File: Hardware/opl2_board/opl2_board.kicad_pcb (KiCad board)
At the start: 2 copper layers, 80.8 x 60.1 mm, 21 parts, among them J1 Conn_01x40, J2 AudioJack3, U1 74HC00, U2 YM3812, U3 YM3014B, U4 LM358, X1 CXO_DIP8

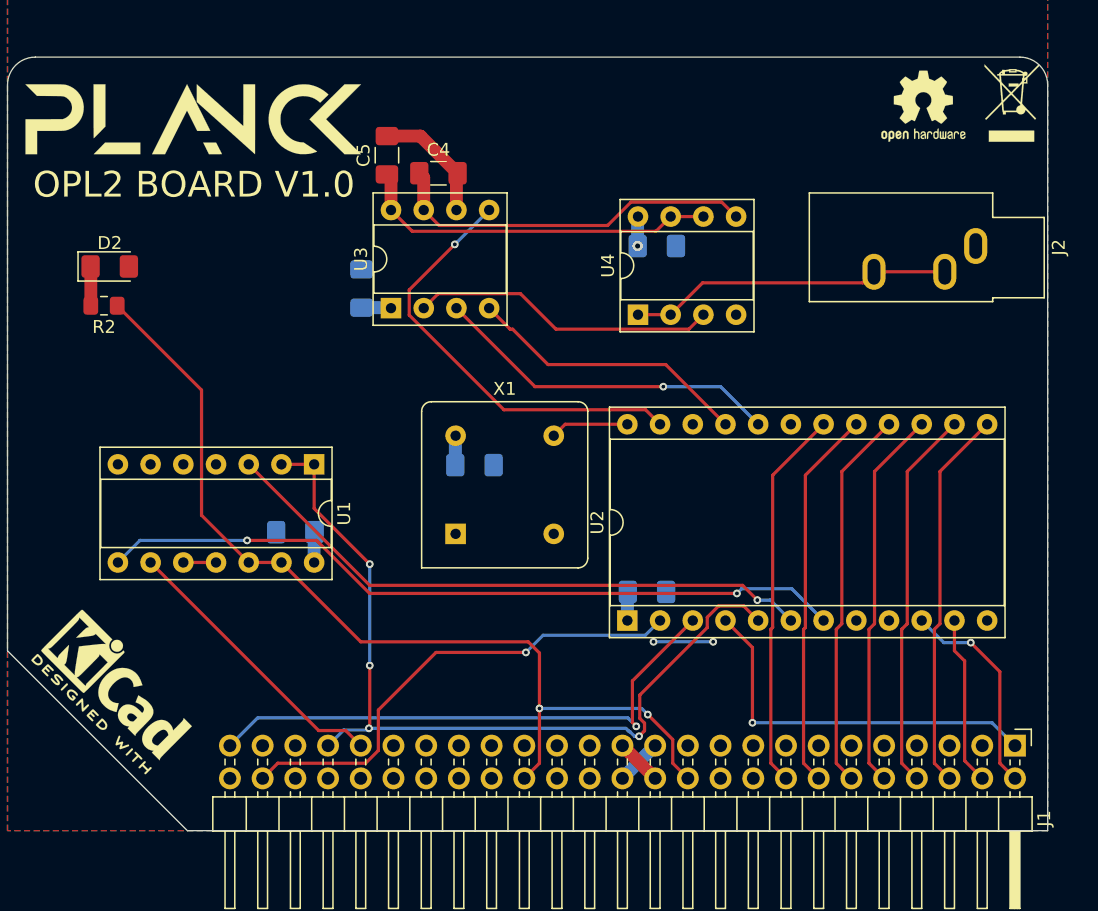
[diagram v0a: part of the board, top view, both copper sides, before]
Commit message: Through hole components for OPL2 board
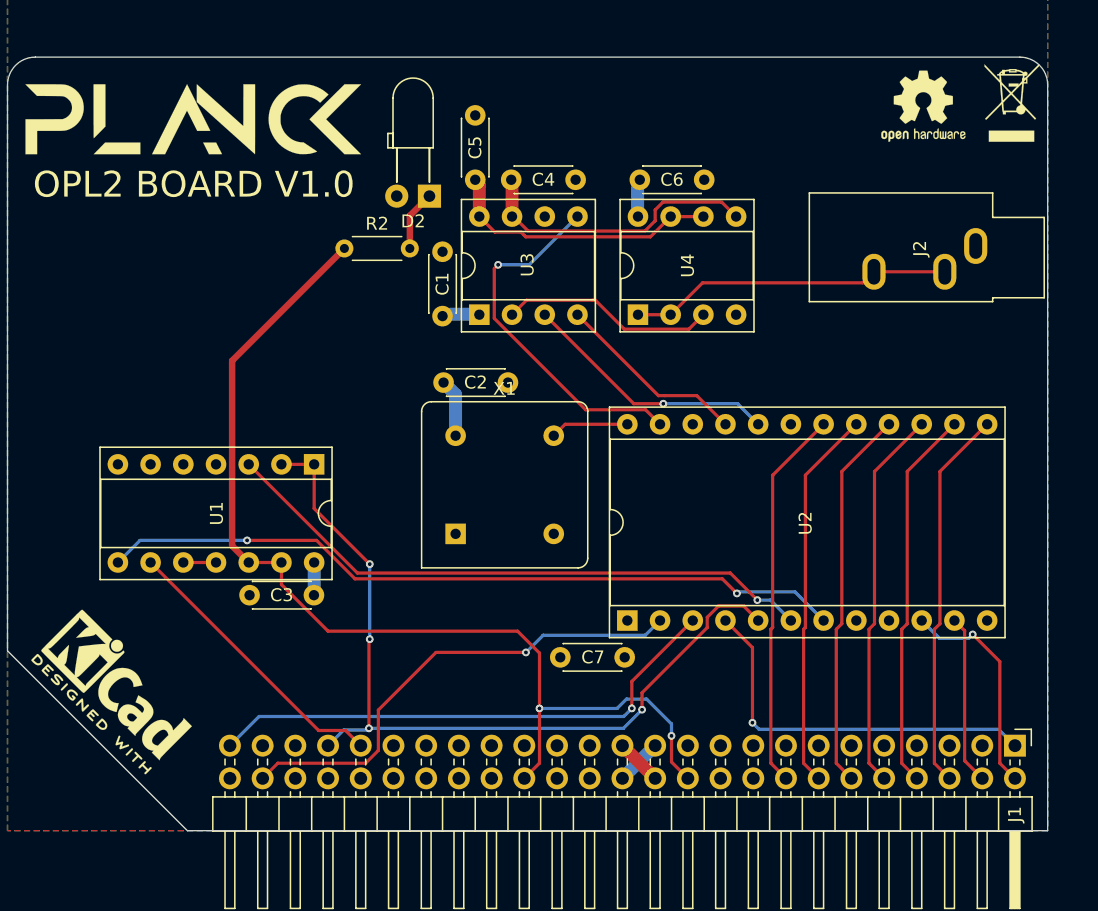
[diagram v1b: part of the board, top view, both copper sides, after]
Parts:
- C1, C2, C3, C6, C7: value C_Small -> 4.7u; footprint Capacitor_SMD:C_1206_3216Metric_Pad1.42x1.75mm_HandSolder -> Capacitor_THT:C_Disc_D4.3mm_W1.9mm_P5.00mm; moved to F.Cu
- C4, C5: footprint Capacitor_SMD:C_1206_3216Metric_Pad1.42x1.75mm_HandSolder -> Capacitor_THT:C_Disc_D4.3mm_W1.9mm_P5.00mm
- D2: footprint LED_SMD:LED_1206_3216Metric_Pad1.42x1.75mm_HandSolder -> LED_THT:LED_D3.0mm_Horizontal_O3.81mm_Z6.0mm
- R2: footprint Resistor_SMD:R_0805_2012Metric_Pad1.15x1.40mm_HandSolder -> Resistor_THT:R_Axial_DIN0204_L3.6mm_D1.6mm_P5.08mm_Horizontal
- X1: value CXO_DIP8 -> 3.579545 MHz
- moved D2 25.4 mm to (32.8, -49.3), turned to 180 degrees
- moved R2 19.2 mm to (26.2, -45.2), turned to 0 degrees
- moved C7 8.43 mm to (42.9, -13.5), turned to 0 degrees
- moved C5 7.12 mm to (36.3, -50.5)
- moved C2 6.92 mm to (38.9, -34.8)
- moved C1 6.91 mm to (33.8, -45.0)
- moved U3 6.88 mm to (36.6, -40.1)
- moved C6 6.33 mm to (54.1, -50.5)
- moved C3 6.05 mm to (18.8, -18.3)
- moved C4 5.67 mm to (39.1, -50.5)
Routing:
- net GND: track 13.2 -> 3.59 mm
- net Net-(U3-Pad2): track 23.8 -> 16.7 mm
- net Net-(U2-Pad21): track 22.1 -> 15.0 mm
- net Net-(U2-Pad20): track 27.2 -> 20.1 mm
- net Net-(C5-Pad1): track 28.3 -> 21.6 mm
- net ~SLOT_SEL~: track 74.7 -> 81.3 mm
- net Net-(C4-Pad1): track 29.0 -> 22.8 mm
- net Net-(U2-Pad23): track 33.7 -> 28.3 mm
- net +5V: track 19.7 -> 15.9 mm, vias 3 -> 0
- net R~W~: track 66.5 -> 64.4 mm
- net ~RESET~: track 43.0 -> 41.2 mm
- net Net-(D2-Pad1): track 3.06 -> 4.70 mm
- net D0: track 16.5 -> 17.2 mm
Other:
- rule pad_to_mask_clearance: 0.05 -> 0

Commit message: bigger resistors on OPL2 board
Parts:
- C1, C2, C3, C6, C7: value 4.7u -> 10n
- R2: footprint Resistor_THT:R_Axial_DIN0204_L3.6mm_D1.6mm_P5.08mm_Horizontal -> Resistor_THT:R_Axial_DIN0207_L6.3mm_D2.5mm_P10.16mm_Horizontal
- moved R2 5.08 mm to (21.1, -45.2)
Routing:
- net ~SLOT_SEL~: track 81.3 -> 79.2 mm

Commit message: don't remember what I did there and diffs are useless :/
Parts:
- moved C3 0.25 mm to (18.8, -18.0)

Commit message: change audio jack footprint
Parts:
- J2: value AudioJack3 -> AudioJack; footprint Connector_Audio:Jack_3.5mm_CUI_SJ1-3533NG_Horizontal -> Connector_Audio:Jack_3.5mm_PJ320E_Horizontal
- moved J2 6.61 mm to (68.6, -45.2)
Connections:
- J2 pad T: Net-(J2-PadR) -> Net-(J2-PadR1)
- U4 pad 1: Net-(J2-PadR) -> Net-(J2-PadR1)
- U4 pad 2: Net-(J2-PadR) -> Net-(J2-PadR1)
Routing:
- net Net-(J2-PadR1): track 0.00 -> 25.8 mm
- net Net-(J2-PadR): track 25.2 -> 0.00 mm

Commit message: update gerbers
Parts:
- removed D2: LED, LED_THT:LED_D3.0mm_Horizontal_O3.81mm_Z6.0mm
- removed R2: 330R, Resistor_THT:R_Axial_DIN0207_L6.3mm_D2.5mm_P10.16mm_Horizontal
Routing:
- net ~SLOT_SEL~: track 79.4 -> 53.0 mm
- net Net-(D2-Pad1): track 4.70 -> 0.00 mm

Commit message: Update opl2 board
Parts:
- removed the G*** at (66.0, -56.0)
- removed the G*** at (14.4, -55.2)
- removed the REF** at (78.0, -56.5)
- added C8: 10u, Capacitor_THT:CP_Radial_D5.0mm_P2.50mm, F.Cu at (150.1, 123.1)
- added G***: LOGO, Logo:logo, F.Cu at (111.1, 80.0)
- added G***: LOGO, Logo:logo, B.Cu at (161.4, 79.4)
- J2: footprint Connector_Audio:Jack_3.5mm_PJ320E_Horizontal -> Keebio-Parts:TRRS-PJ-320A-no-Fmask
- moved J2 171.9 mm to (174.4, 90.3)
- moved REF** 166.9 mm to (104.9, 125.2)
- moved J1 166.2 mm to (173.9, 129.3)
- moved C1 166.2 mm to (129.4, 90.9)
- moved C4 166.2 mm to (134.7, 85.3)
- moved C2 166.2 mm to (134.5, 101.1)
- moved C3 166.2 mm to (114.4, 117.9)
- moved C5 166.2 mm to (132.0, 85.3)
- moved C6 166.2 mm to (149.7, 85.3)
- moved C7 166.2 mm to (138.6, 122.4)
- moved U1 166.2 mm to (119.4, 107.4)
- moved U2 166.2 mm to (143.8, 119.6)
- moved U3 166.2 mm to (132.3, 95.8)
- moved U4 166.2 mm to (144.6, 95.8)
- moved X1 166.2 mm to (130.4, 112.8)
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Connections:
- net R~W~ renamed R~{W}
- net ~INH~ renamed ~{INH}
- net ~IRQ~ renamed ~{IRQ}
- net ~NMI~ renamed ~{NMI}
- net ~RESET~ renamed ~{RESET}
- net ~SLOT_IRQ~ renamed ~{SLOT_IRQ}
- net ~SLOT_SEL~ renamed ~{SLOT_SEL}
- net ~SSEL~ renamed ~{SSEL}
- J2 pad R2: GND -> Net-(J2-PadR1)
- J2 pad S: GND -> Net-(J2-PadR1)
- J2 pad T: Net-(J2-PadR1) -> GND
- U1 pad 6: Net-(U1-Pad6) -> unconnected-(U1-Pad6)
- X1 pad 1: Net-(X1-Pad1) -> unconnected-(X1-Pad1)
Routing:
- net Net-(J2-PadR1): track 25.8 -> 32.6 mm
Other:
- net class Default removed
- board text added: "OPL2 BOARD ${VERSION}"
- board text removed: "OPL2 BOARD V1.0"
